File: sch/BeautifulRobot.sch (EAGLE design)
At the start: 10 parts, among them IC1 STC12C4052AD, Q1 12MHz

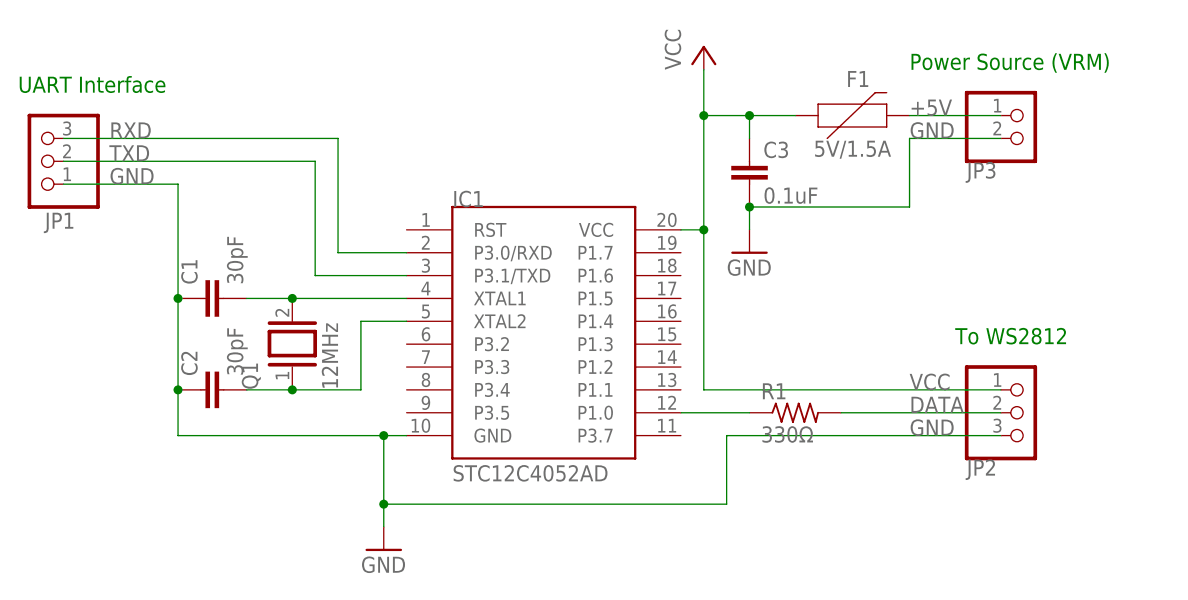
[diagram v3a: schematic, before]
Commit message: Update schematic to add new indicator light
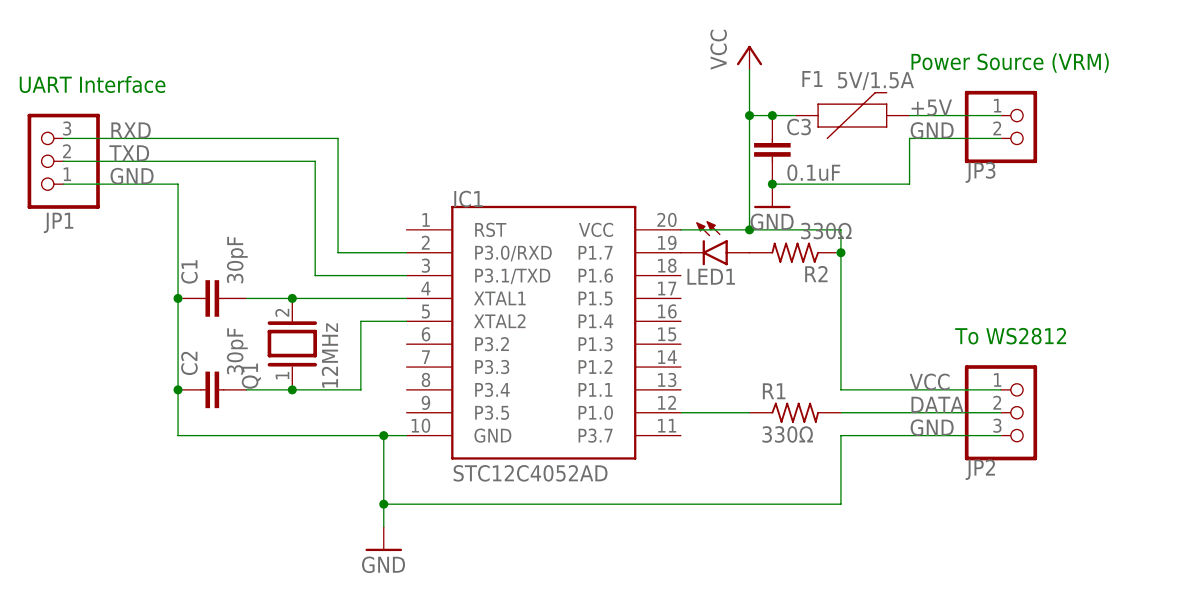
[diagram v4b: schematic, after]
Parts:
- added LED1: (no value), led:LED5MM
- added R2: 330Ω, rcl:R-US_0204/7
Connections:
- new net N$5: LED1.A, R2.2
- new net N$6: IC1.P1.7, LED1.C
- net VCC: now also R2.1
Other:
- moved on the sheet: C3
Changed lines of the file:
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@@
 <part name="C3" library="rcl" library_urn="urn:adsk.eagle:library:334" deviceset="C-EU" device="025-025X050" package3d_urn="urn:adsk.eagle:package:23629/2" value="0.1uF"/>
 <part name="R1" library="rcl" library_urn="urn:adsk.eagle:library:334" deviceset="R-US_" device="0204/7" package3d_urn="urn:adsk.eagle:package:23498/2" value="330Ω"/>
+<part name="LED1" library="led" library_urn="urn:adsk.eagle:library:259" deviceset="LED" device="5MM" package3d_urn="urn:adsk.eagle:package:15799/2"/>
+<part name="R2" library="rcl" library_urn="urn:adsk.eagle:library:334" deviceset="R-US_" device="0204/7" package3d_urn="urn:adsk.eagle:package:23498/2" value="330Ω"/>
 </parts>
 <sheets>
@@
 <attribute name="VALUE" x="119.38" y="73.66" size="1.778" layer="96"/>
 </instance>
-<instance part="P+1" gate="VCC" x="147.32" y="121.92" smashed="yes">
-<attribute name="VALUE" x="144.78" y="119.38" size="1.778" layer="96" rot="R90"/>
+<instance part="P+1" gate="VCC" x="152.4" y="121.92" smashed="yes">
+<attribute name="VALUE" x="149.86" y="119.38" size="1.778" layer="96" rot="R90"/>
 </instance>
 <instance part="GND1" gate="1" x="111.76" y="66.04" smashed="yes">
@@
 </instance>
 <instance part="F1" gate="G$1" x="162.56" y="114.3" smashed="yes">
-<attribute name="NAME" x="164.465" y="117.475" size="1.778" layer="95" font="vector" align="bottom-center"/>
-<attribute name="VALUE" x="163.83" y="111.506" size="1.778" layer="96" font="vector" align="top-center"/>
-</instance>
-<instance part="GND2" gate="1" x="152.4" y="99.06" smashed="yes">
-<attribute name="VALUE" x="149.86" y="96.52" size="1.778" layer="96"/>
-</instance>
-<instance part="C3" gate="G$1" x="152.4" y="109.22" smashed="yes">
-<attribute name="NAME" x="153.924" y="109.601" size="1.778" layer="95"/>
-<attribute name="VALUE" x="153.924" y="104.521" size="1.778" layer="96"/>
+<attribute name="NAME" x="159.385" y="117.475" size="1.778" layer="95" font="vector" align="bottom-center"/>
+<attribute name="VALUE" x="166.37" y="119.126" size="1.778" layer="96" font="vector" align="top-center"/>
+</instance>
+<instance part="GND2" gate="1" x="154.94" y="104.14" smashed="yes">
+<attribute name="VALUE" x="152.4" y="101.6" size="1.778" layer="96"/>
+</instance>
+<instance part="C3" gate="G$1" x="154.94" y="111.76" smashed="yes">
+<attribute name="NAME" x="156.464" y="112.141" size="1.778" layer="95"/>
+<attribute name="VALUE" x="156.464" y="107.061" size="1.778" layer="96"/>
 </instance>
 <instance part="R1" gate="G$1" x="157.48" y="81.28" smashed="yes">
 <attribute name="NAME" x="153.67" y="82.7786" size="1.778" layer="95"/>
 <attribute name="VALUE" x="153.67" y="77.978" size="1.778" layer="96"/>
+</instance>
+<instance part="LED1" gate="G$1" x="149.86" y="99.06" smashed="yes" rot="R270">
+<attribute name="NAME" x="145.288" y="95.504" size="1.778" layer="95"/>
+<attribute name="VALUE" x="145.288" y="93.345" size="1.778" layer="96"/>
+</instance>
+<instance part="R2" gate="G$1" x="157.48" y="99.06" smashed="yes" rot="R180">
+<attribute name="NAME" x="161.29" y="97.5614" size="1.778" layer="95" rot="R180"/>
+<attribute name="VALUE" x="163.83" y="102.362" size="1.778" layer="96" rot="R180"/>
 </instance>
 </instances>
@@
 <pinref part="GND1" gate="1" pin="GND"/>
 <wire x1="111.76" y1="68.58" x2="111.76" y2="71.12" width="0.1524" layer="91"/>
-<pinref part="JP2" gate="A" pin="3"/>
-<wire x1="180.34" y1="78.74" x2="149.86" y2="78.74" width="0.1524" layer="91"/>
-<wire x1="149.86" y1="78.74" x2="149.86" y2="71.12" width="0.1524" layer="91"/>
-<wire x1="149.86" y1="71.12" x2="111.76" y2="71.12" width="0.1524" layer="91"/>
+<wire x1="162.56" y1="71.12" x2="111.76" y2="71.12" width="0.1524" layer="91"/>
 <label x="170.18" y="78.74" size="1.778" layer="95"/>
 <pinref part="IC1" gate="G$1" pin="GND"/>
@@
 <junction x="111.76" y="71.12"/>
 <junction x="111.76" y="78.74"/>
+<pinref part="JP2" gate="A" pin="3"/>
+<wire x1="180.34" y1="78.74" x2="162.56" y2="78.74" width="0.1524" layer="91"/>
+<wire x1="162.56" y1="78.74" x2="162.56" y2="71.12" width="0.1524" layer="91"/>
 </segment>
 <segment>
@@
 <pinref part="JP3" gate="G$1" pin="2"/>
 <wire x1="180.34" y1="111.76" x2="170.18" y2="111.76" width="0.1524" layer="91"/>
-<wire x1="170.18" y1="111.76" x2="170.18" y2="104.14" width="0.1524" layer="91"/>
+<wire x1="170.18" y1="111.76" x2="170.18" y2="106.68" width="0.1524" layer="91"/>
 <label x="170.18" y="111.76" size="1.778" layer="95"/>
-<wire x1="170.18" y1="104.14" x2="152.4" y2="104.14" width="0.1524" layer="91"/>
-<junction x="152.4" y="104.14"/>
-<wire x1="152.4" y1="104.14" x2="152.4" y2="101.6" width="0.1524" layer="91"/>
+<wire x1="170.18" y1="106.68" x2="154.94" y2="106.68" width="0.1524" layer="91"/>
+<junction x="154.94" y="106.68"/>
 </segment>
 </net>
@@
 <segment>
 <pinref part="P+1" gate="VCC" pin="VCC"/>
-<wire x1="147.32" y1="114.3" x2="147.32" y2="119.38" width="0.1524" layer="91"/>
-<wire x1="157.48" y1="114.3" x2="152.4" y2="114.3" width="0.1524" layer="91"/>
-<pinref part="IC1" gate="G$1" pin="VCC"/>
-<wire x1="152.4" y1="114.3" x2="147.32" y2="114.3" width="0.1524" layer="91"/>
-<wire x1="147.32" y1="101.6" x2="144.78" y2="101.6" width="0.1524" layer="91"/>
-<wire x1="147.32" y1="114.3" x2="147.32" y2="101.6" width="0.1524" layer="91"/>
-<junction x="147.32" y="114.3"/>
+<wire x1="152.4" y1="114.3" x2="152.4" y2="119.38" width="0.1524" layer="91"/>
 <pinref part="F1" gate="G$1" pin="1"/>
 <pinref part="C3" gate="G$1" pin="1"/>
-<wire x1="152.4" y1="111.76" x2="152.4" y2="114.3" width="0.1524" layer="91"/>
+<junction x="154.94" y="114.3"/>
+<wire x1="154.94" y1="114.3" x2="157.48" y2="114.3" width="0.1524" layer="91"/>
+<wire x1="154.94" y1="114.3" x2="152.4" y2="114.3" width="0.1524" layer="91"/>
+<label x="170.18" y="83.82" size="1.778" layer="95"/>
+<pinref part="JP2" gate="A" pin="1"/>
+<wire x1="180.34" y1="83.82" x2="162.56" y2="83.82" width="0.1524" layer="91"/>
+<wire x1="162.56" y1="83.82" x2="162.56" y2="99.06" width="0.1524" layer="91"/>
+<pinref part="IC1" gate="G$1" pin="VCC"/>
+<wire x1="162.56" y1="99.06" x2="162.56" y2="101.6" width="0.1524" layer="91"/>
+<wire x1="162.56" y1="101.6" x2="152.4" y2="101.6" width="0.1524" layer="91"/>
+<wire x1="152.4" y1="101.6" x2="144.78" y2="101.6" width="0.1524" layer="91"/>
+<wire x1="152.4" y1="114.3" x2="152.4" y2="101.6" width="0.1524" layer="91"/>
 <junction x="152.4" y="114.3"/>
-<pinref part="JP2" gate="A" pin="1"/>
-<label x="170.18" y="83.82" size="1.778" layer="95"/>
-<wire x1="180.34" y1="83.82" x2="147.32" y2="83.82" width="0.1524" layer="91"/>
-<wire x1="147.32" y1="83.82" x2="147.32" y2="101.6" width="0.1524" layer="91"/>
-<junction x="147.32" y="101.6"/>
+<junction x="152.4" y="101.6"/>
+<pinref part="R2" gate="G$1" pin="1"/>
+<junction x="162.56" y="99.06"/>
 </segment>
 </net>
@@
 </segment>
 </net>
+<net name="N$5" class="0">
+<segment>
+<pinref part="R2" gate="G$1" pin="2"/>
+<pinref part="LED1" gate="G$1" pin="A"/>
+</segment>
+</net>
+<net name="N$6" class="0">
+<segment>
+<pinref part="LED1" gate="G$1" pin="C"/>
+<pinref part="IC1" gate="G$1" pin="P1.7"/>
+</segment>
+</net>
